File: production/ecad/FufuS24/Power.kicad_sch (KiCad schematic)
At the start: 0 parts

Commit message: updated footprint library
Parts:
- added U4: ~, footprints:DPAK114P990X239-6N, symbol tps78533qkvurq1:TPS78533QKVURQ1
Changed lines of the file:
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@@
 (kicad_sch (version 20230121) (generator eeschema)
   (paper "A4")
+  (symbol (lib_id "tps78533qkvurq1:TPS78533QKVURQ1") (at 132.08 81.28 0) (unit 1)
+    (in_bom yes) (on_board yes) (dnp no) (fields_autoplaced)
+    (property "Reference" "U4" (at 134.62 80.01 0)
+      (effects (font (size 1.27 1.27)))
+    )
+    (property "Value" "~" (at 132.08 81.28 0)
+      (effects (font (size 1.27 1.27)))
+    )
+    (property "Footprint" "footprints:DPAK114P990X239-6N" (at 132.08 81.28 0)
+      (effects (font (size 1.27 1.27)) hide)
+    )
+    (property "Datasheet" "" (at 132.08 81.28 0)
+      (effects (font (size 1.27 1.27)) hide)
+    )
+    (pin "1")
+    (pin "4")
+    (pin "5")
+    (pin "3")
+    (pin "2")
+    (instances
+      (project "FufuS24"
+        (path "/c4c3980b-c8c0-435e-abdc-bbed2349d7ac/1f62379a-1fa8-439b-93cd-7c736b3b1bba"
+          (reference "U4") (unit 1)
+        )
+      )
+    )
+  )
 )

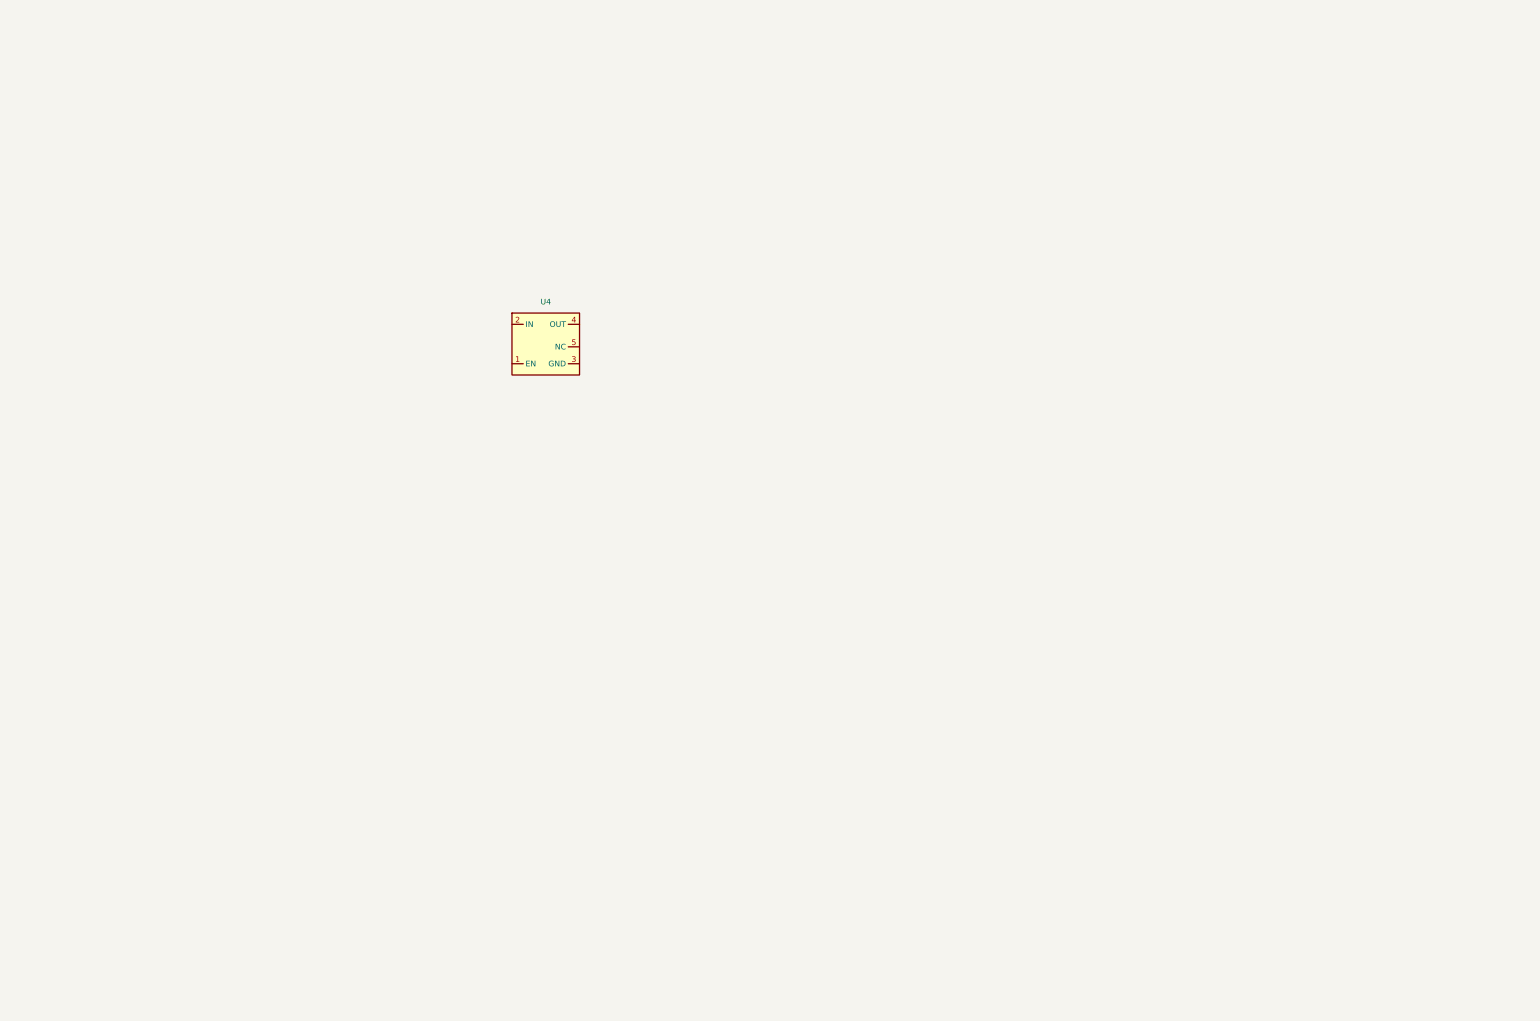
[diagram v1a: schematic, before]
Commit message: Added new modules and finished first draft of 16V converter
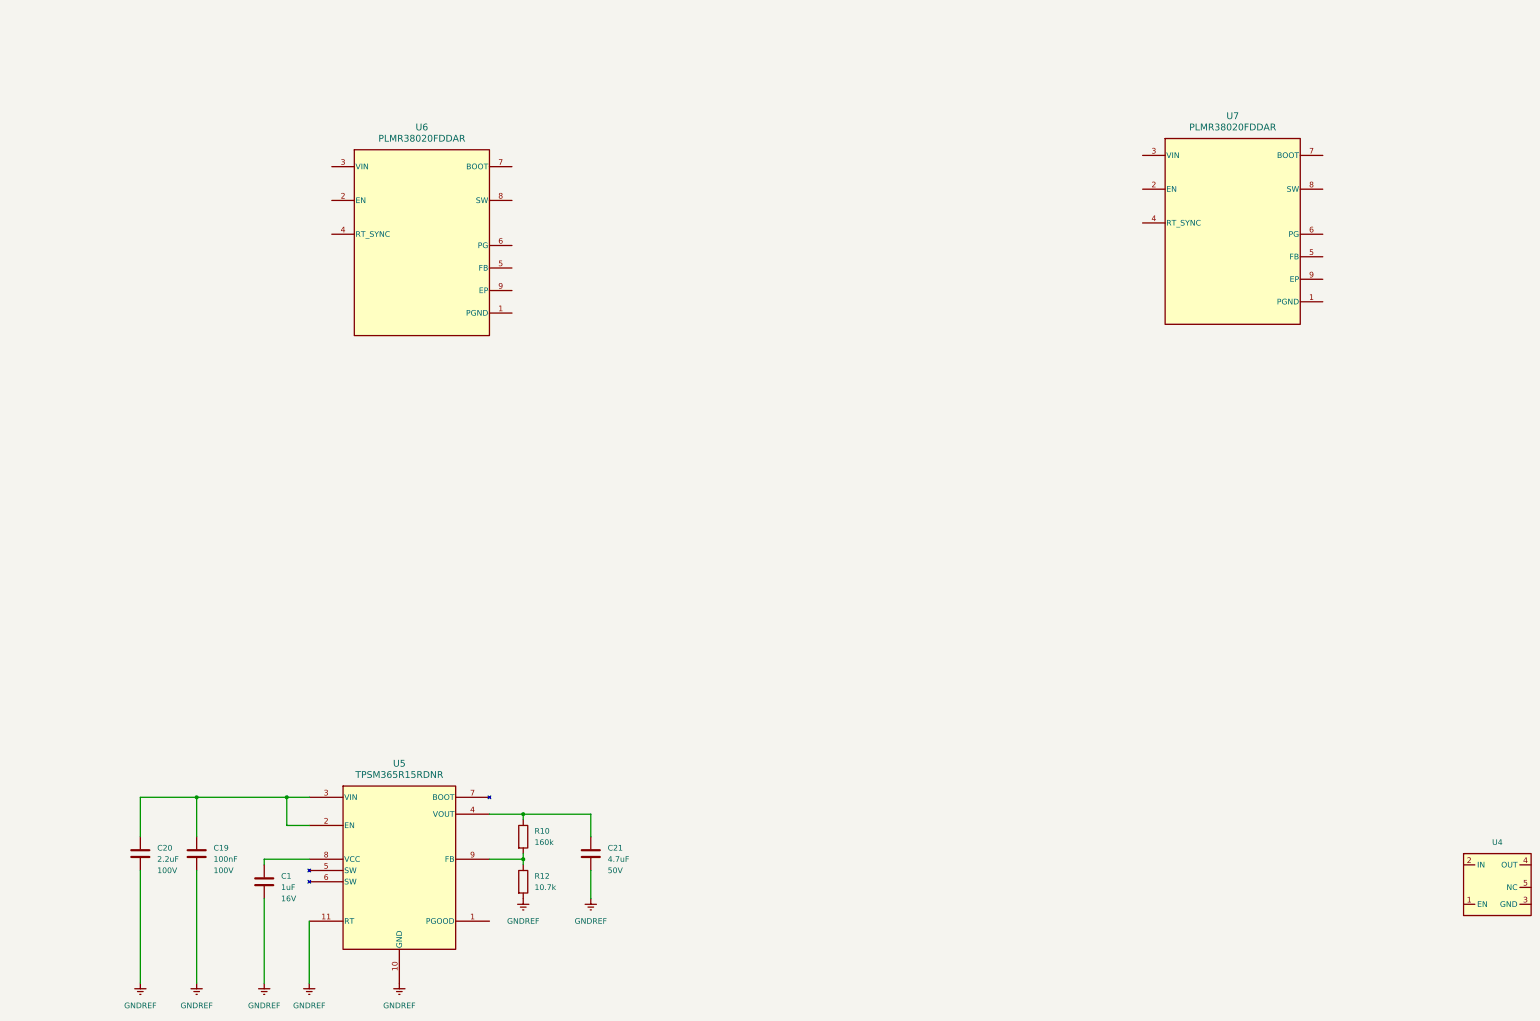
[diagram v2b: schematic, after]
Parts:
- added C1: 1uF, symbol Device:C
- added C19: 100nF, symbol Device:C
- added C20: 2.2uF, symbol Device:C
- added C21: 4.7uF, symbol Device:C
- added R10: 160k, symbol Device:R
- added R12: 10.7k, symbol Device:R
- added U5: TPSM365R15RDNR, footprints:QFN-FCMOD_365R6FRDN_TEX, symbol TPSM365R15RDNR:TPSM365R15RDNR
- added U6, U7: PLMR38020FDDAR, footprints:DDA0008E-MFG, symbol LMR38020FDDAR:PLMR38020FDDAR
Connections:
- new net: C21.1, R10.1, U5.4 (VOUT)
- new net: R10.2, R12.1, U5.9 (FB)
- new net: C19.1, C20.1, U5.2 (EN), U5.3 (VIN)
- new net: C1.1, U5.8 (VCC)
- new net GNDREF: C1.2, C19.2, C20.2, C21.2, R12.2, U5.10 (GND), U5.11 (RT)
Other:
- moved on the sheet: U4

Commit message: worked on power page
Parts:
- added C22: 100nF, symbol Device:C
- added C23, C24, C25: 10uF, symbol CL21A106KAYNNNG:CL21A106KAYNNNG
- added L2: CDRH127_LDNP-330MC, footprints:INDPM120120X800N, symbol CDRH127_LDNP-330MC:CDRH127_LDNP-330MC
- added R13: 110k, symbol Device:R
- added R14: 10k, symbol Device:R
- added R15: 64.9k, symbol Device:R
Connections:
- net GNDREF: now also U6.1 (PGND), U6.9 (EP), C23.2, C24.2, C25.2, R14.2, R15.2
- net +16V: now reaches C21.1, R10.1, U5.4 (VOUT)
- net +48V: now reaches C19.1, C20.1, U5.2 (EN), U5.3 (VIN)
- net +48V: now also U6.2 (EN), U6.3 (VIN)
- net at U6.4 (RT_SYNC): now also R15.1
- net at U6.5 (FB): now also R13.2, R14.1
- net at U6.7 (BOOT): now also C22.1
- net at U6.8 (SW): now also C22.2, L2.1
- new net +12V: C23.1, C24.1, C25.1, L2.2, R13.1
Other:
- moved on the sheet: C1, C19, C20, C21, R10, R12, U4, U5, U6, U7

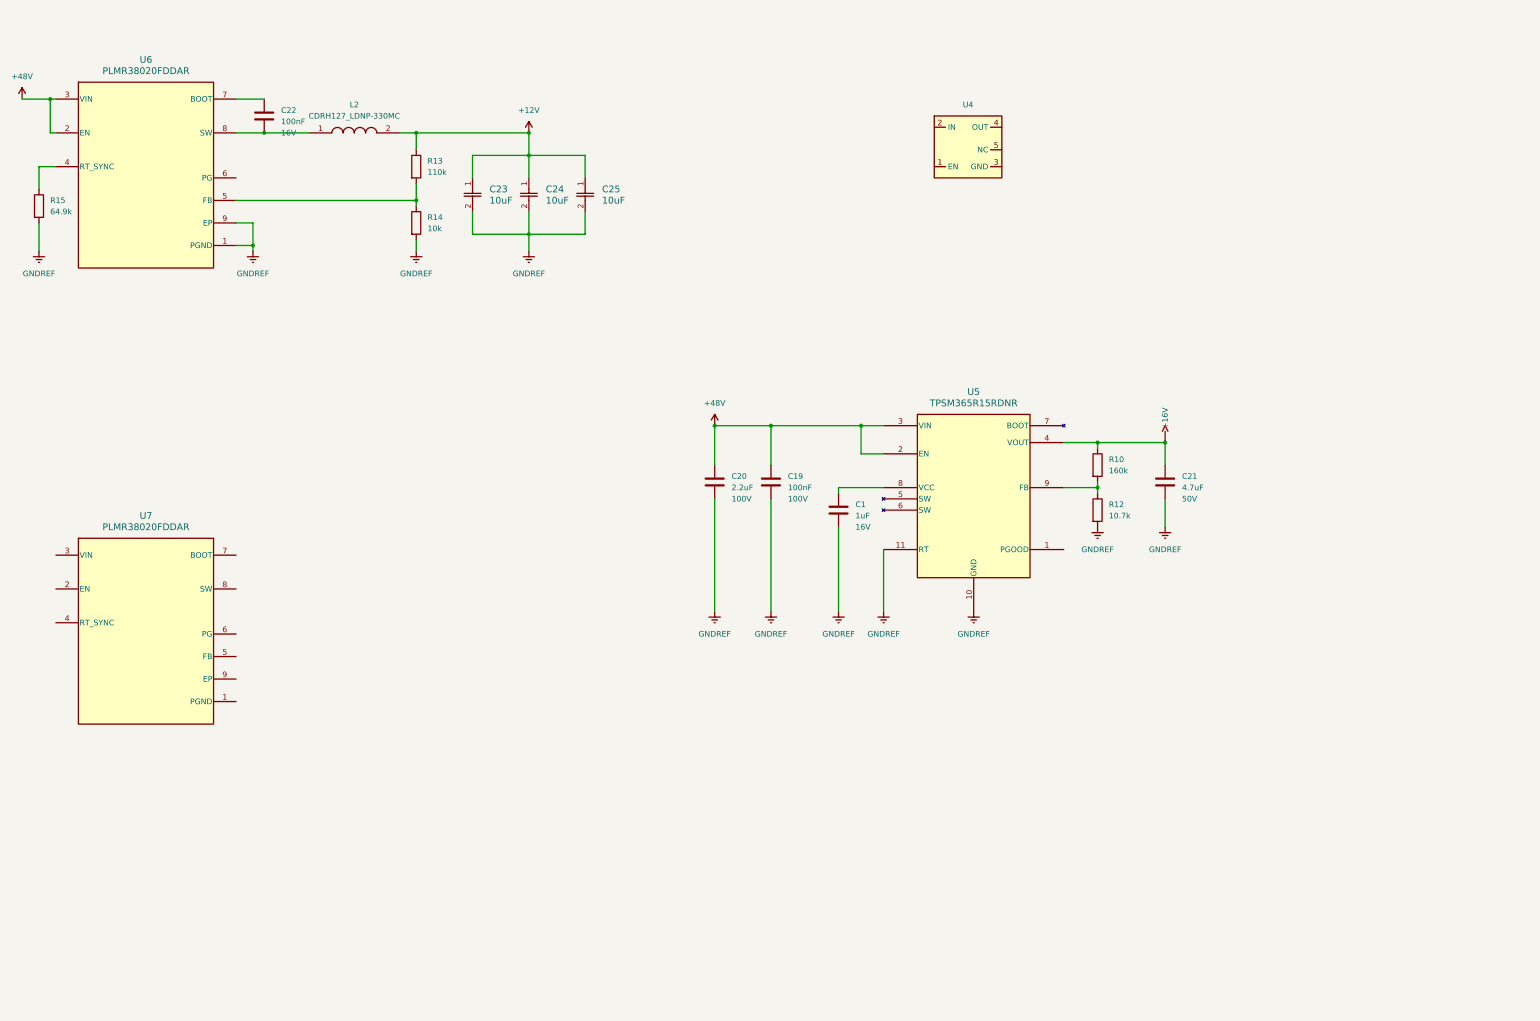
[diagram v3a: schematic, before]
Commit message: Finished first draft of power page
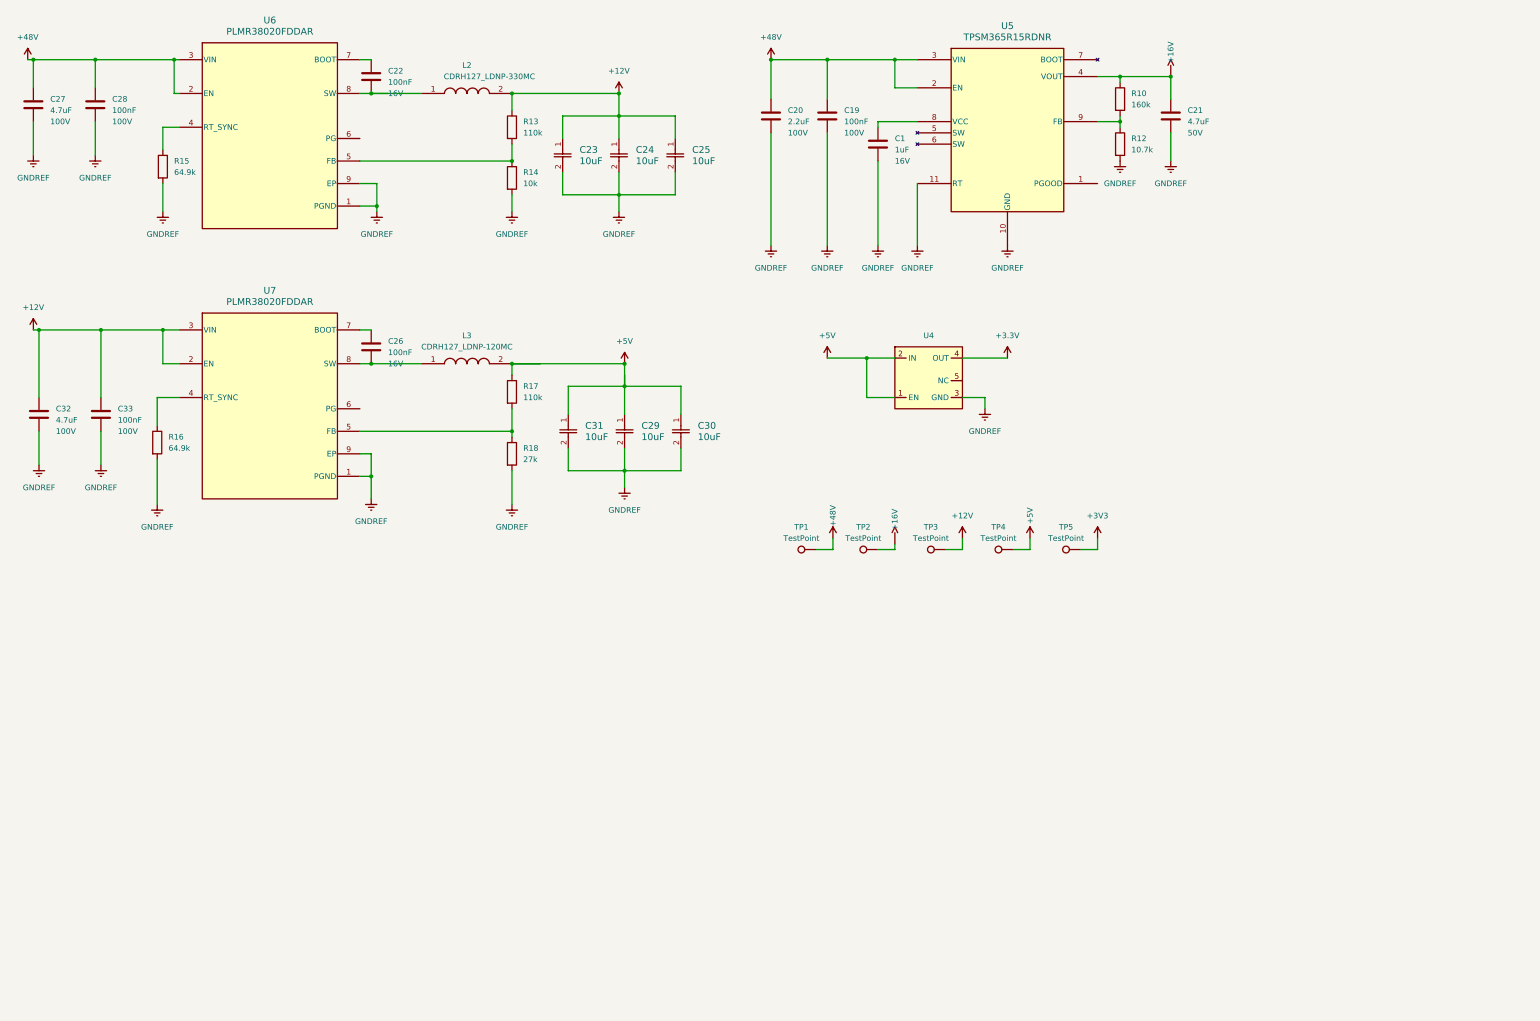
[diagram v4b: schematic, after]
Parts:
- added C26, C28, C33: 100nF, symbol Device:C
- added C27, C32: 4.7uF, symbol Device:C
- added C29, C30, C31: 10uF, symbol CL21A106KAYNNNG:CL21A106KAYNNNG
- added L3: CDRH127_LDNP-120MC, INDPM120120X800N, symbol CDRH127_LDNP-120MC:CDRH127_LDNP-120MC
- added R16: 64.9k, symbol Device:R
- added R17: 110k, symbol Device:R
- added R18: 27k, symbol Device:R
- added TP1, TP2, TP3, TP4, TP5: TestPoint, TestPoint:TestPoint_Pad_2.0x2.0mm, symbol Connector:TestPoint
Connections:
- net +12V: now also U7.2 (EN), U7.3 (VIN), C32.1, C33.1, TP3.1
- net +16V: now also TP2.1
- net +48V: now also C27.1, C28.1, TP1.1
- net GNDREF: now also U4.3 (GND), U7.1 (PGND), U7.9 (EP), C27.2, C28.2, C29.2, C30.2, C31.2, C32.2, C33.2, R16.2, R18.2
- net +5V: now reaches U4.1 (EN)
- net +5V: now also U4.2 (IN), C29.1, C30.1, C31.1, L3.2, R17.1, TP4.1
- net +3.3V: now reaches U4.4 (OUT)
- net at U7.4 (RT_SYNC): now also R16.1
- net at U7.5 (FB): now also R17.2, R18.1
- net at U7.7 (BOOT): now also C26.1
- net at U7.8 (SW): now also C26.2, L3.1
- new net +3V3: TP5.1
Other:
- moved on the sheet: C1, C19, C20, C21, C22, C23, C24, C25, L2, R10, R12, R13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

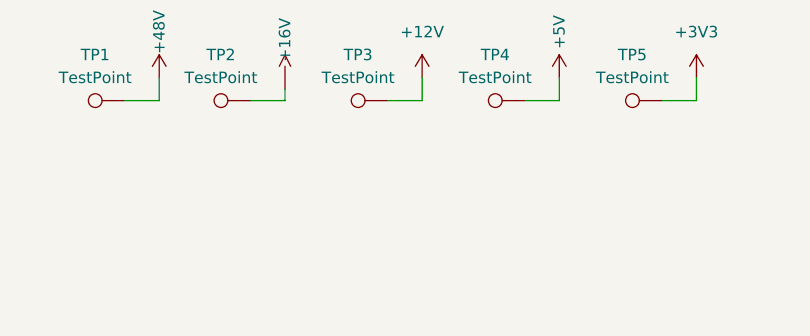
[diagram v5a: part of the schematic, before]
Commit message: Design review changes
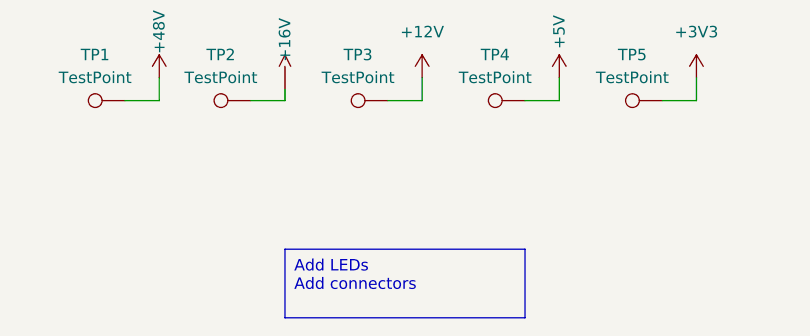
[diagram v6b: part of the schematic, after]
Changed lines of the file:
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@@
     (stroke (width 0) (type default))
+  )
+  (text_box "Add LEDs\nAdd connectors"
+    (at 213.36 152.4 0) (size 26.67 7.62)
+    (stroke (width 0) (type default))
+    (fill (type none))
+    (effects (font (size 1.27 1.27)) (justify left top))
   )
   (symbol (lib_id "CL21A106KAYNNNG:CL21A106KAYNNNG") (at 151.13 43.18 270) (unit 1)

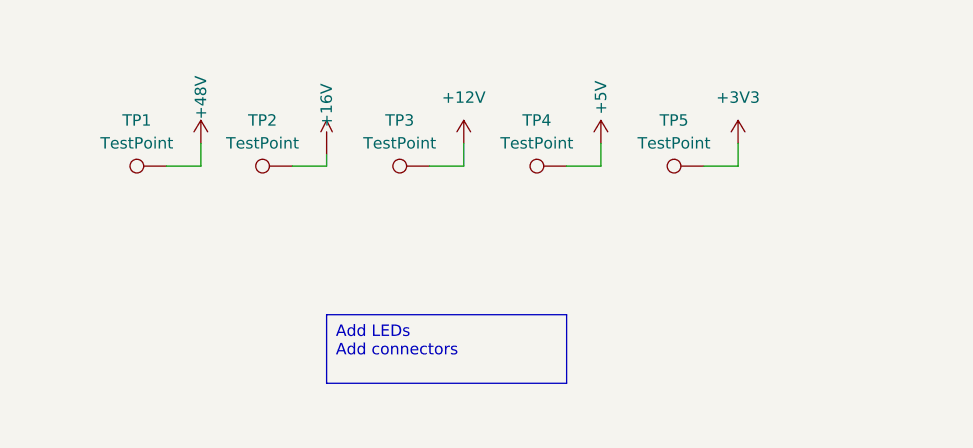
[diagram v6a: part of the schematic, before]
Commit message: added LEDs
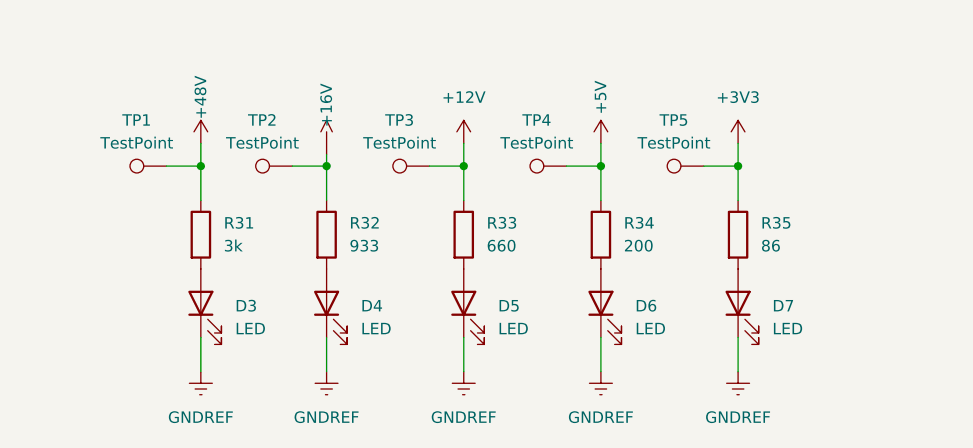
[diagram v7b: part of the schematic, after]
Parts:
- added D3, D4, D5, D6, D7: LED, symbol Device:LED
- added R31: 3k, symbol Device:R
- added R32: 933, symbol Device:R
- added R33: 660, symbol Device:R
- added R34: 200, symbol Device:R
- added R35: 86, symbol Device:R
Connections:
- net +12V: now also R33.1
- net +16V: now also R32.1
- net +3V3: now also R35.1
- net +48V: now also R31.1
- net +5V: now also R34.1
- net GNDREF: now also D3.1 (K), D4.1 (K), D5.1 (K), D6.1 (K), D7.1 (K)
- new net: D4.2 (A), R32.2
- new net: D7.2 (A), R35.2
- new net: D3.2 (A), R31.2
- new net: D5.2 (A), R33.2
- new net: D6.2 (A), R34.2
